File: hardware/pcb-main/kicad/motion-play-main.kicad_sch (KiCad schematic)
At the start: 12 parts, among them J3 LED_Strip, J4 Conn_01x05, J5 Conn_01x05, J6 Conn_01x05

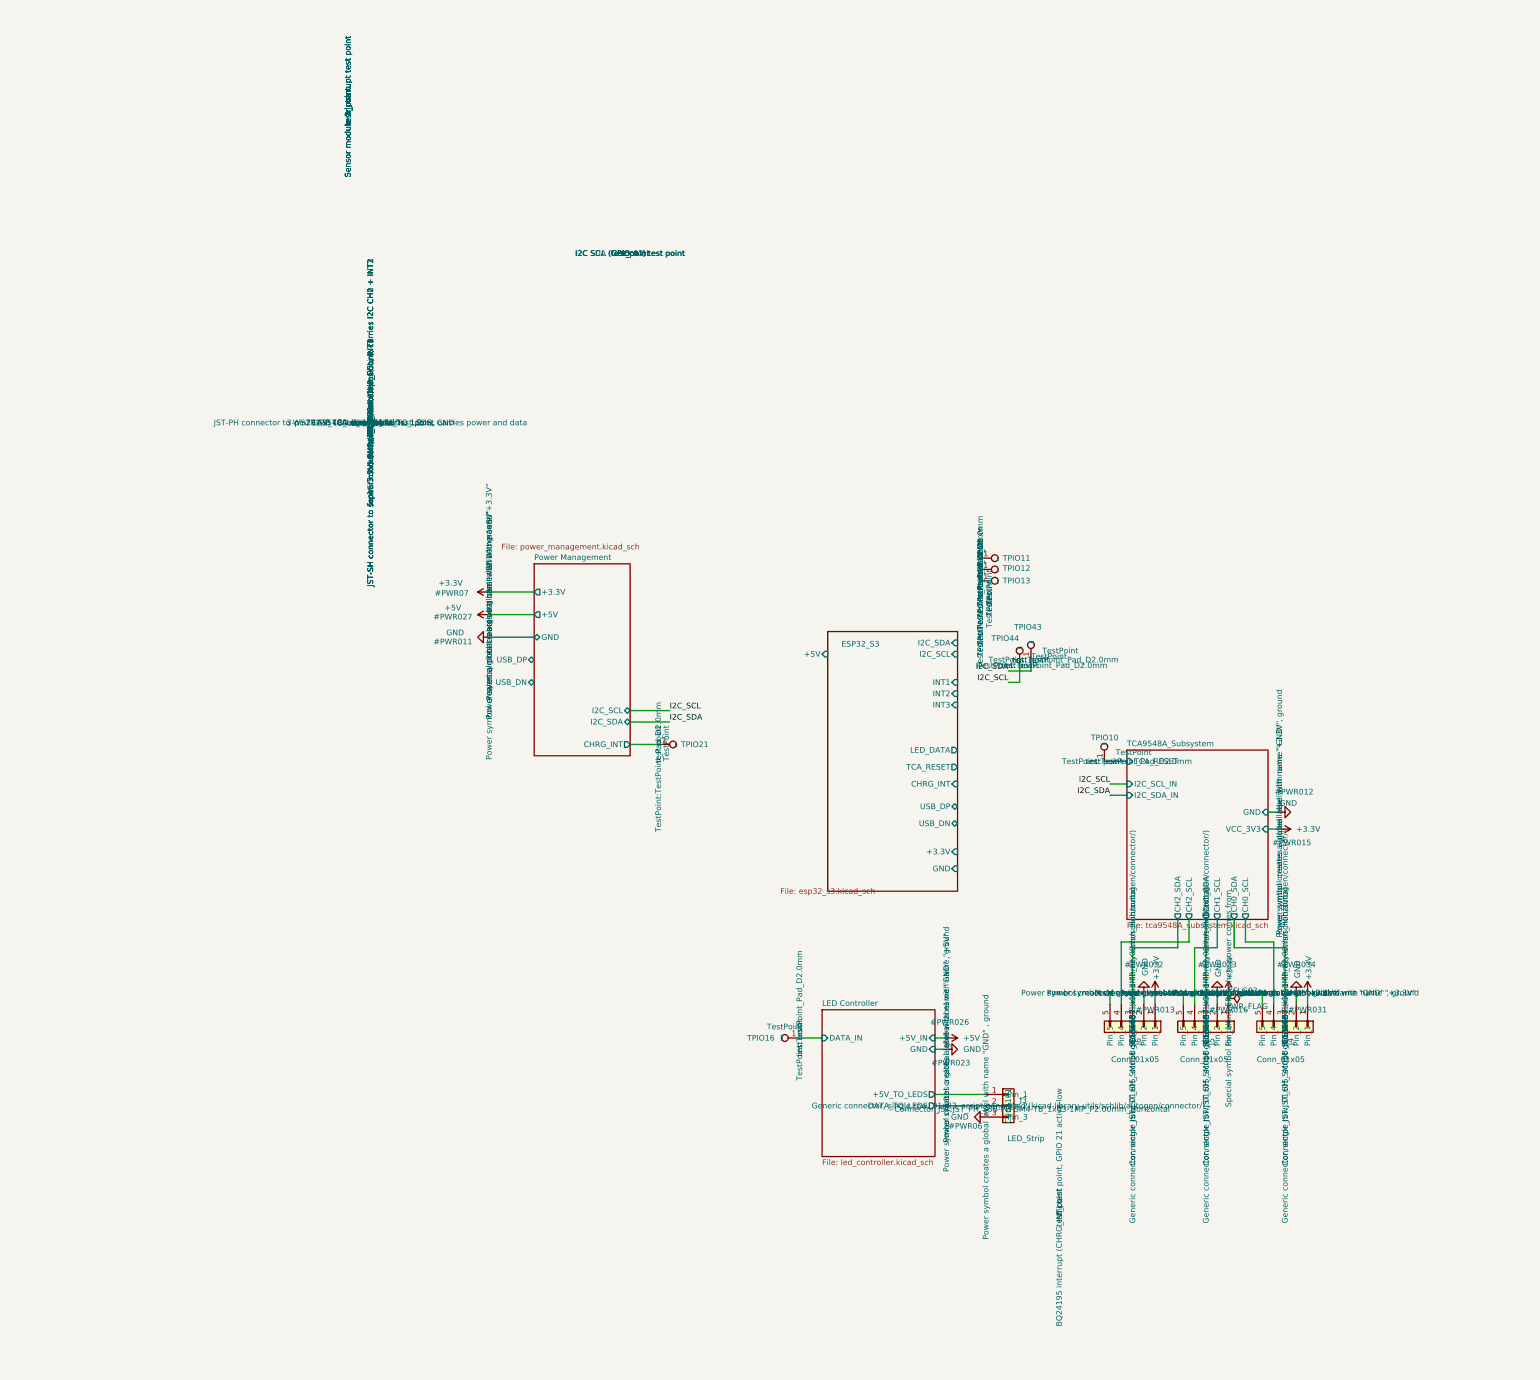
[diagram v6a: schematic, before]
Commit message: Complete Phase 1d/1e: manual wiring, ERC clean (0 errors)
Root sheet:
- Wire ESP32_S3 sheet pins to system nets via labels (I2C_SDA,
  I2C_SCL, TCA_RESET, LED_DATA, CHRG_INT, USB_DP, USB_DN)
- Connect power pins with +3.3V, +5V, GND power symbols
- Add PWR_FLAG symbols to resolve power-not-driven ERC errors
- NC flags on INT1/2/3 (design decision to drop interrupt lines)
- Remove TPIO11/12/13 (INT test points, no longer needed)
- Clean up dangling wires from old U2/U1 area
- Remove stray I2C_SCL hierarchical label

Power management sheet:
- Wire J7 D+/D- pads (A6/B6 tied to USB_DP, A7/B7 tied to USB_DN)
- Insert VSYS_SW into power path: R44 and INA219 IN+ now on
  VSYS_SW net so SW1 actually disconnects boost converter input
- Position AMS1117, caps, USBLC6, power switch components

ESP32_S3 sheet:
- Add no-connect on D5 DOUT (status LED has no downstream chain)
- Component positioning cleanup

ERC: 0 errors, 69 warnings (all benign JLC-MCP pin type mismatches
and footprint library path issues)

Made-with: Cursor
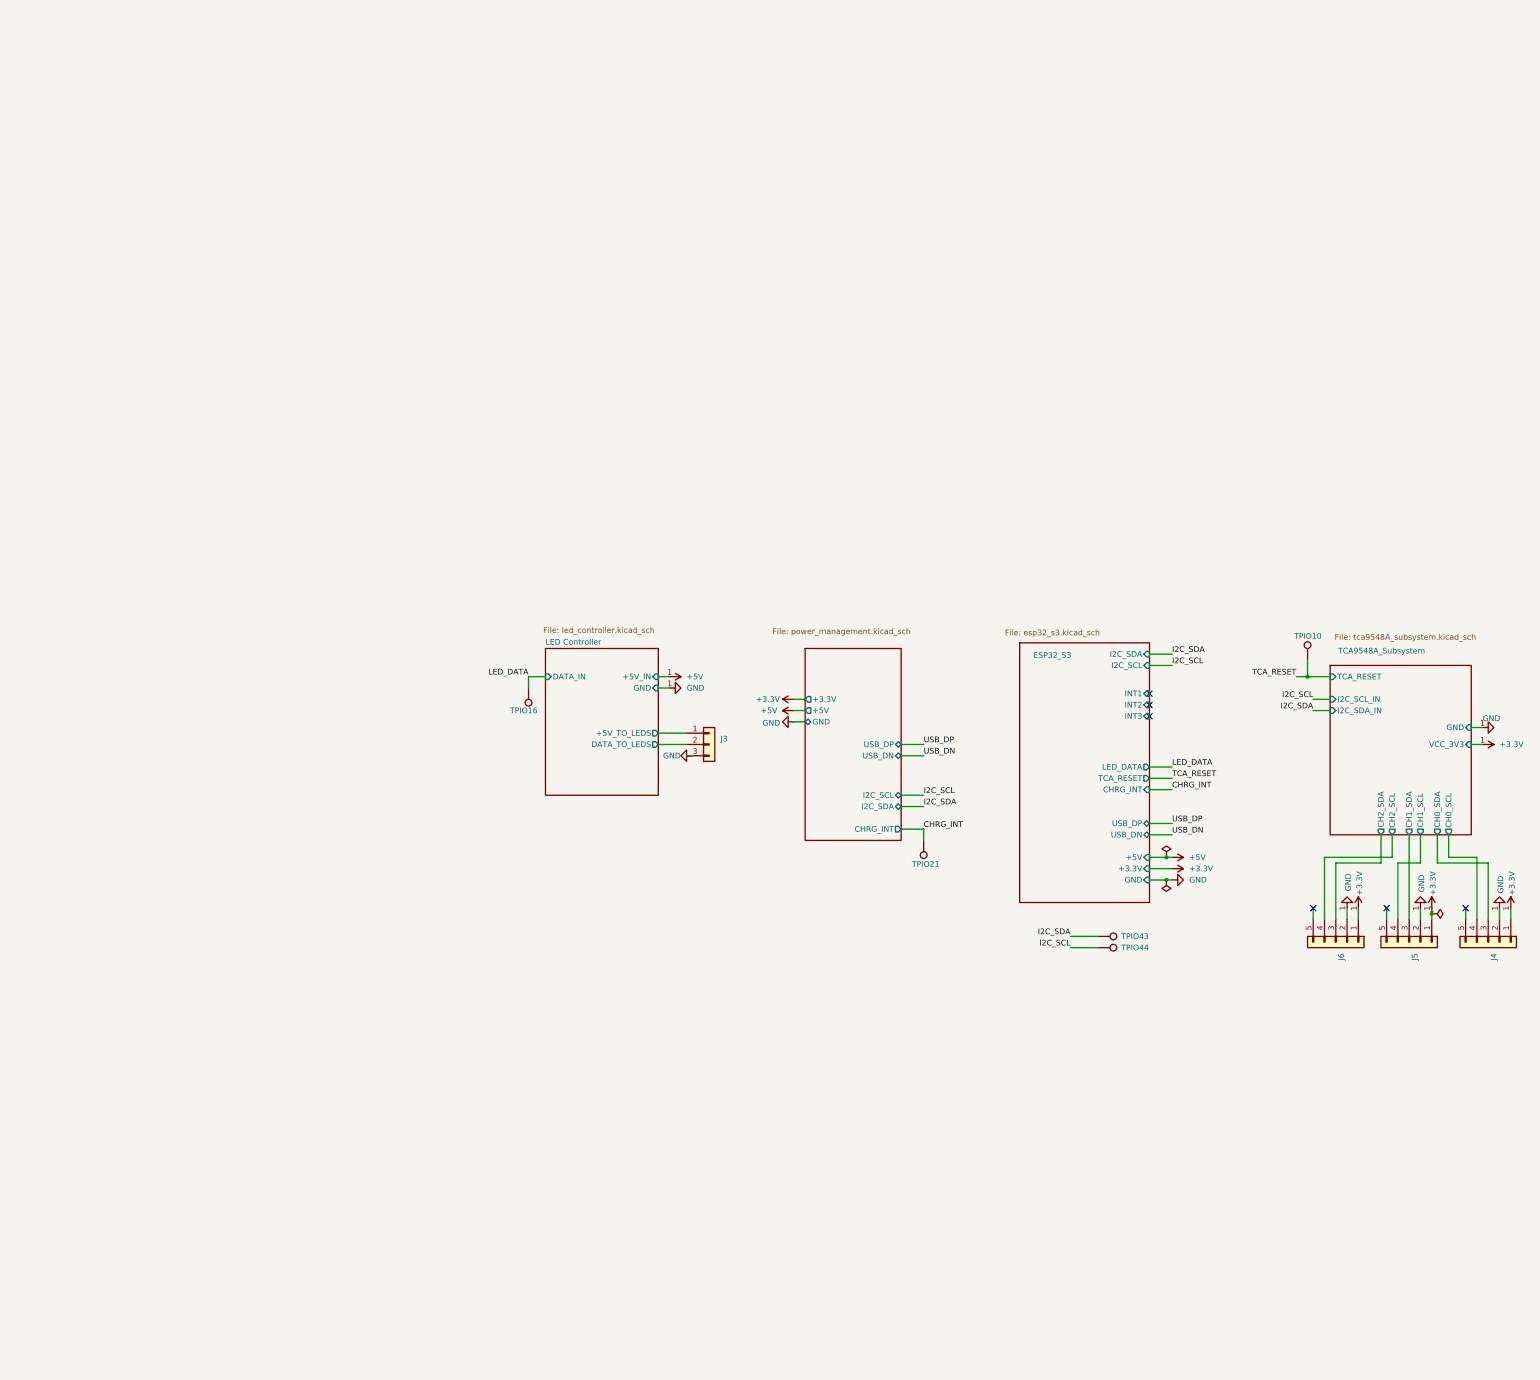
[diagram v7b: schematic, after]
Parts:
- removed TPIO11, TPIO12, TPIO13: TestPoint, TestPoint:TestPoint_Pad_D2.0mm, symbol Connector:TestPoint
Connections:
- net LED Controller/DATA_IN renamed LED_DATA
- net Power Management/CHRG_INT renamed CHRG_INT
- net TCA9548A_Subsystem/TCA_RESET renamed TCA_RESET
- no-connect marks 3 -> 6

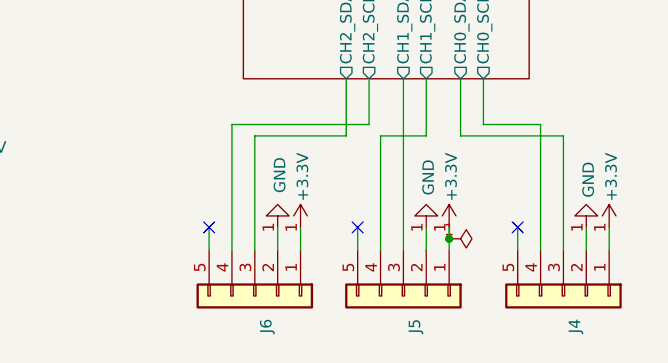
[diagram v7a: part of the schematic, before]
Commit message: Hardware revision: remove interrupts, update connectors, add DIP switch
Remove INT lines from all three PCBs (main, rigid, flex). Replace 5-pin
JST-SH connectors with 4-pin SM04B-SRSS-TB on main and rigid boards.
Replace solder jumpers with EP-02KS DIP switch for I2C address config
on rigid board. Update FPC connector pinout to remove INT signals and
add GND fills. Update stiffener specs (PI 0.25mm tail, SS 0.2mm IC
areas). Regenerate production files (BOM, CPL) for both sensor boards.
Update hardware CONTEXT.md with corrected addresses (0x74-0x76),
component tables, and pinouts.

Made-with: Cursor
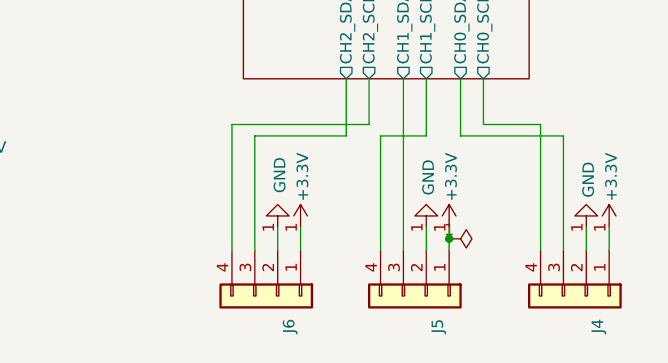
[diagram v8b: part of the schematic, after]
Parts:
- J4: value Conn_01x05 -> Conn_01x04; footprint Connector_JST:JST_SH_SM05B-SRSS-TB_1x05-1MP_P1.00mm_Horizontal -> Connector_JST:JST_SH_SM04B-SRSS-TB_1x04-1MP_P1.00mm_Horizontal; symbol Connector_Generic:Conn_01x05 -> Connector_Generic:Conn_01x04; LCSC Part C136657 -> C160404; LCSC Part No C136657 -> C160404; ai_critical_specs 5-pin: 3.3V, GND, CH0_SDA, CH0_SCL, INT1 -> 4-pin: 3.3V, GND, CH0_SDA, CH0_SCL; ai_function JST-SH connector to sensor module 1 (M1, 6 oclock position), carries I2C CH0 + INT1 -> JST-SH connector to sensor module 1 (M1, 6 oclock position), carries I2C CH0
- J5: value Conn_01x05 -> Conn_01x04; footprint Connector_JST:JST_SH_SM05B-SRSS-TB_1x05-1MP_P1.00mm_Horizontal -> Connector_JST:JST_SH_SM04B-SRSS-TB_1x04-1MP_P1.00mm_Horizontal; symbol Connector_Generic:Conn_01x05 -> Connector_Generic:Conn_01x04; LCSC Part C136657 -> C160404; LCSC Part No C136657 -> C160404; ai_critical_specs 5-pin: 3.3V, GND, CH1_SDA, CH1_SCL, INT2 -> 4-pin: 3.3V, GND, CH1_SDA, CH1_SCL; ai_function JST-SH connector to sensor module 2 (M2, 9 oclock position), carries I2C CH1 + INT2 -> JST-SH connector to sensor module 2 (M2, 9 oclock position), carries I2C CH1
- J6: value Conn_01x05 -> Conn_01x04; footprint Connector_JST:JST_SH_SM05B-SRSS-TB_1x05-1MP_P1.00mm_Horizontal -> Connector_JST:JST_SH_SM04B-SRSS-TB_1x04-1MP_P1.00mm_Horizontal; symbol Connector_Generic:Conn_01x05 -> Connector_Generic:Conn_01x04; LCSC Part C136657 -> C160404; LCSC Part No C136657 -> C160404; ai_critical_specs 5-pin: 3.3V, GND, CH2_SDA, CH2_SCL, INT3 -> 4-pin: 3.3V, GND, CH2_SDA, CH2_SCL; ai_function JST-SH connector to sensor module 3 (M3, 3 oclock position), carries I2C CH2 + INT3 -> JST-SH connector to sensor module 3 (M3, 3 oclock position), carries I2C CH2
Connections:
- no-connect marks 6 -> 3
